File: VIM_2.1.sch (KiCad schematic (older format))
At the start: 13 parts, among them J1 BARREL_JACK, J2 Sliding switch, U14 LD1117, U8 lm2596 - 5v, U9 LD1117S33CTR

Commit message: added text
added sushil changes
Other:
- note added: "VIM"
- note added: "sushil changes"
- note removed: "ublox m8u"
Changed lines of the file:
@@
 LIBS:mpu
 LIBS:68 PIN
-LIBS:reugulators
 LIBS:simcard
 LIBS:j502
@@
 $EndComp
 Text Notes 1750 3900 0    118  ~ 0
-ublox m8u
+VIM
 $Comp
 L +12V #PWR09
@@
 	5110 3900 5110 3690
 Connection ~ 5110 3690
+Text Notes 3580 5890 0    315  ~ 0
+sushil changes
 $EndSCHEMATC

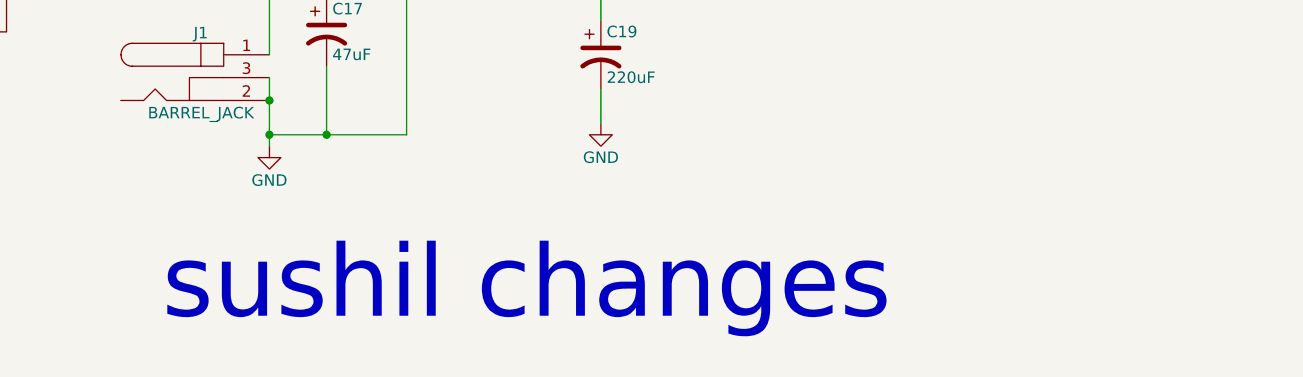
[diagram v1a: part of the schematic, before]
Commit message: Final pcb given to pcbpower
fleet management vim with following features
- ublox m8u, mc60
- mpu6050
- vibration sensor
- buzzer, switches, thottle bypass,
- sim interface according to quectel
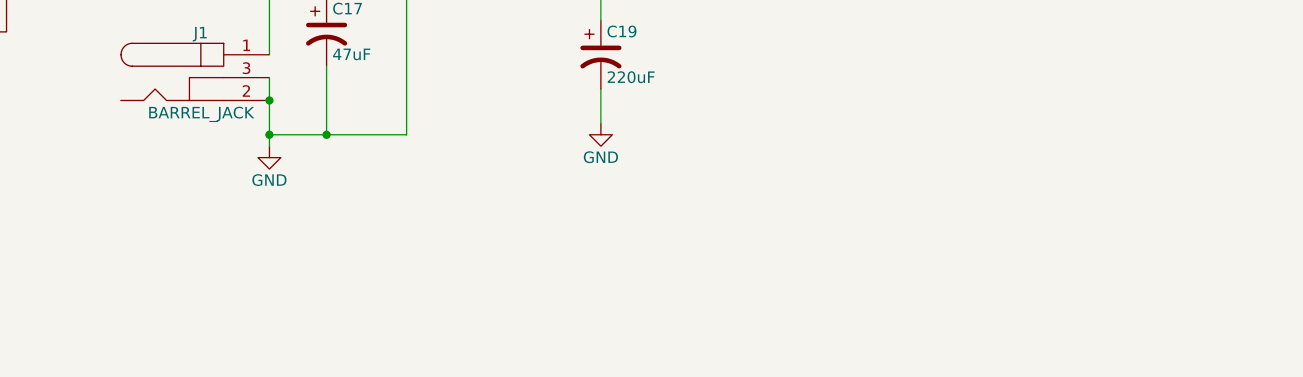
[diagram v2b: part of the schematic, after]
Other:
- note removed: "sushil changes"
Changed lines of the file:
@@
 LIBS:mpu
 LIBS:68 PIN
+LIBS:reugulators
 LIBS:simcard
 LIBS:j502
@@
 	5110 3900 5110 3690
 Connection ~ 5110 3690
-Text Notes 3580 5890 0    315  ~ 0
-sushil changes
 $EndSCHEMATC
